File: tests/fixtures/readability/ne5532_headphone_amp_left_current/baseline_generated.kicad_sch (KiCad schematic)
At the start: 13 parts, among them J1 AudioIn_L, J2 AudioIn_R, J3 PowerSupply, J4 HeadphoneOut_L, J5 HeadphoneOut_R

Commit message: fix: improve layout regression handling
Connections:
- net VCC is gone; now on net GND: J3.1 (A), R3.1 (A), R3.2 (B)
- net GND: now also J4.1 (A), J4.2 (B), J5.1 (A), J5.2 (B), R4.1 (A), R4.2 (B), R7.2 (B), R8.2 (B)
- net at J1.1 (A), J1.2 (B), R1.1 (A): now also J3.2 (B)
- net at R2.2 (B): now also R6.1 (A), R7.1 (A), R8.1 (A)
- now unconnected: R1.2 (B), R5.1 (A), R5.2 (B)

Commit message: fix: stabilize graphviz layout regressions
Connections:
- net GND: now also J3.2 (B); no longer J2.1 (A), J2.2 (B), J3.1 (A), J4.1 (A), J4.2 (B), J5.1 (A), J5.2 (B), R2.1 (A), R3.1 (A), R3.2 (B), R4.1 (A), R7.2 (B), R8.2 (B)
- net at R2.2 (B), R6.1 (A), R8.1 (A): no longer R7.1 (A)
- net at J1.1 (A), J1.2 (B), R1.1 (A): no longer J3.2 (B)
- net VCC: now reaches R1.2 (B)
- net VCC: now also J3.1 (A), R3.1 (A), R3.2 (B), R4.1 (A), R5.1 (A), R7.1 (A)
- new net: J4.1 (A), J4.2 (B), R7.2 (B)
- new net: J2.1 (A), J2.2 (B), R2.1 (A)
- new net: J5.1 (A), J5.2 (B), R8.2 (B)

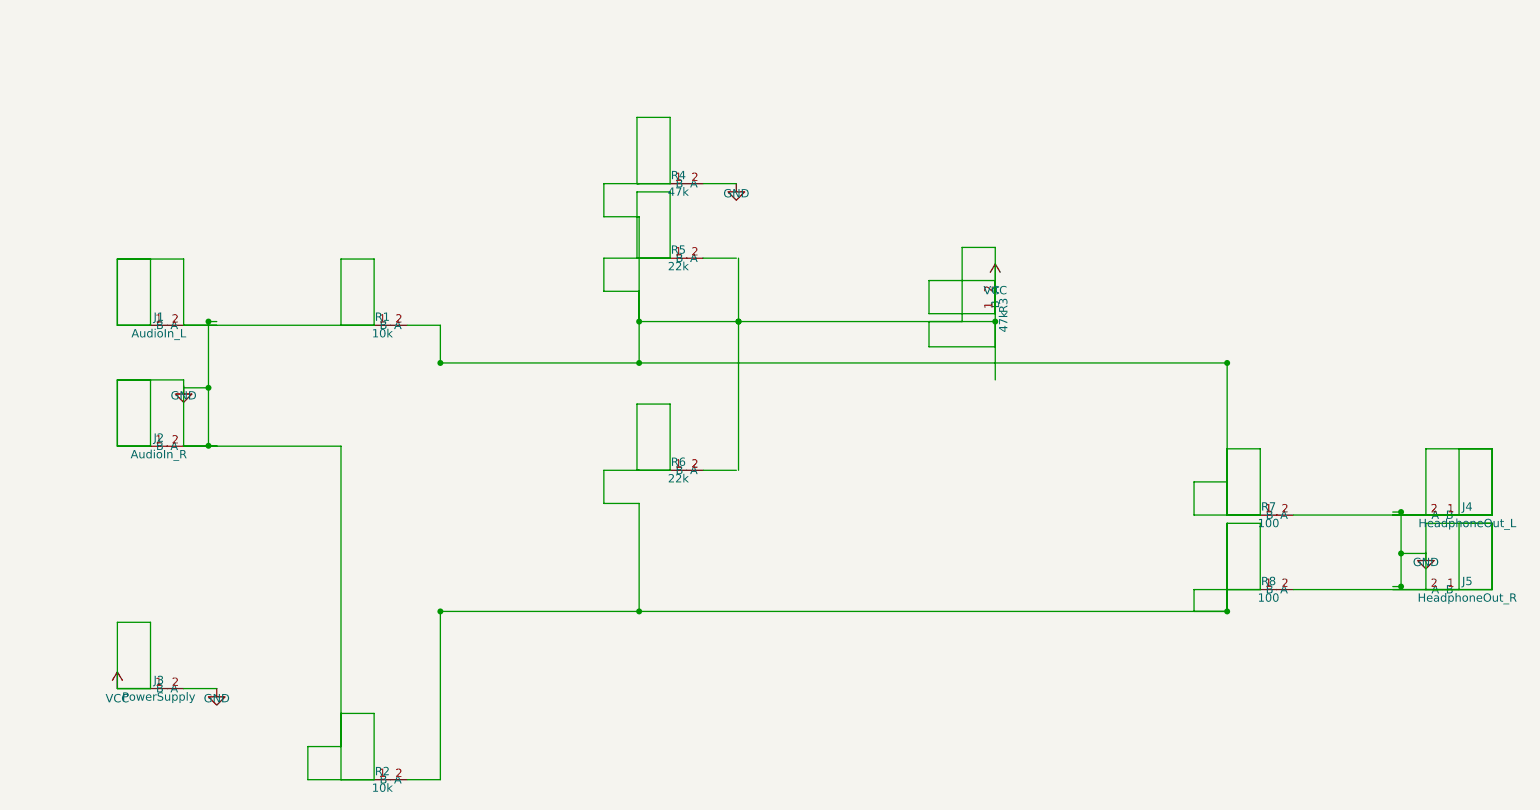
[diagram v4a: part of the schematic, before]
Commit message: fix: refine NE5532 routing geometry
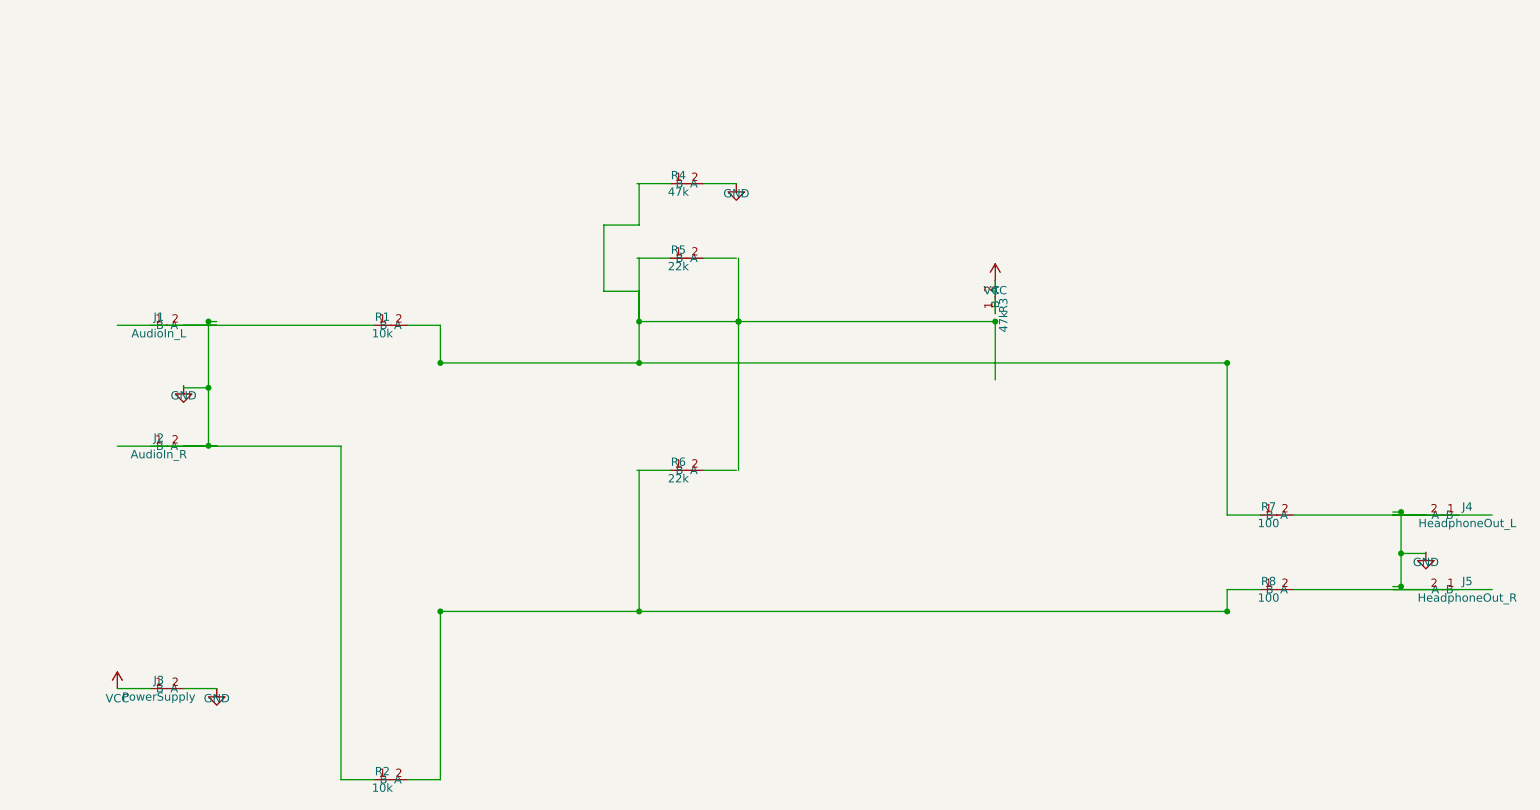
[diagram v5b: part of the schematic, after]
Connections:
- net VCC: no longer R1.2 (B), R4.1 (A), R5.1 (A), R7.1 (A)
- net at J2.2 (B), R2.1 (A): no longer J2.1 (A)
- net at J4.2 (B), R7.2 (B): no longer J4.1 (A)
- net at R2.2 (B), R8.1 (A): no longer R6.1 (A)
- net at J1.2 (B), R1.1 (A): no longer J1.1 (A)
- net at J5.2 (B), R8.2 (B): no longer J5.1 (A)
- new net: R1.2 (B), R7.1 (A)

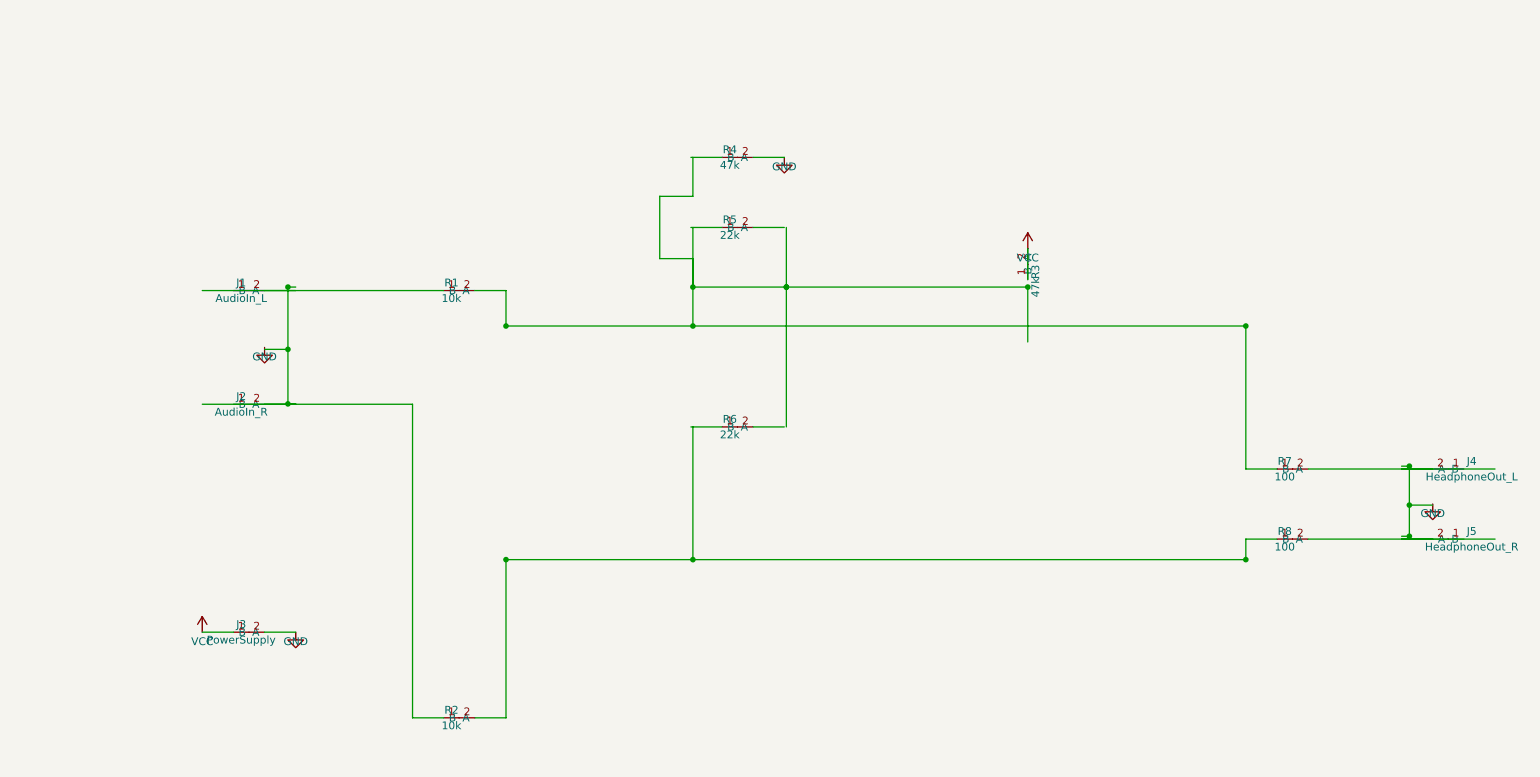
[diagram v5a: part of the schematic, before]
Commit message: fix: improve routing and label readability
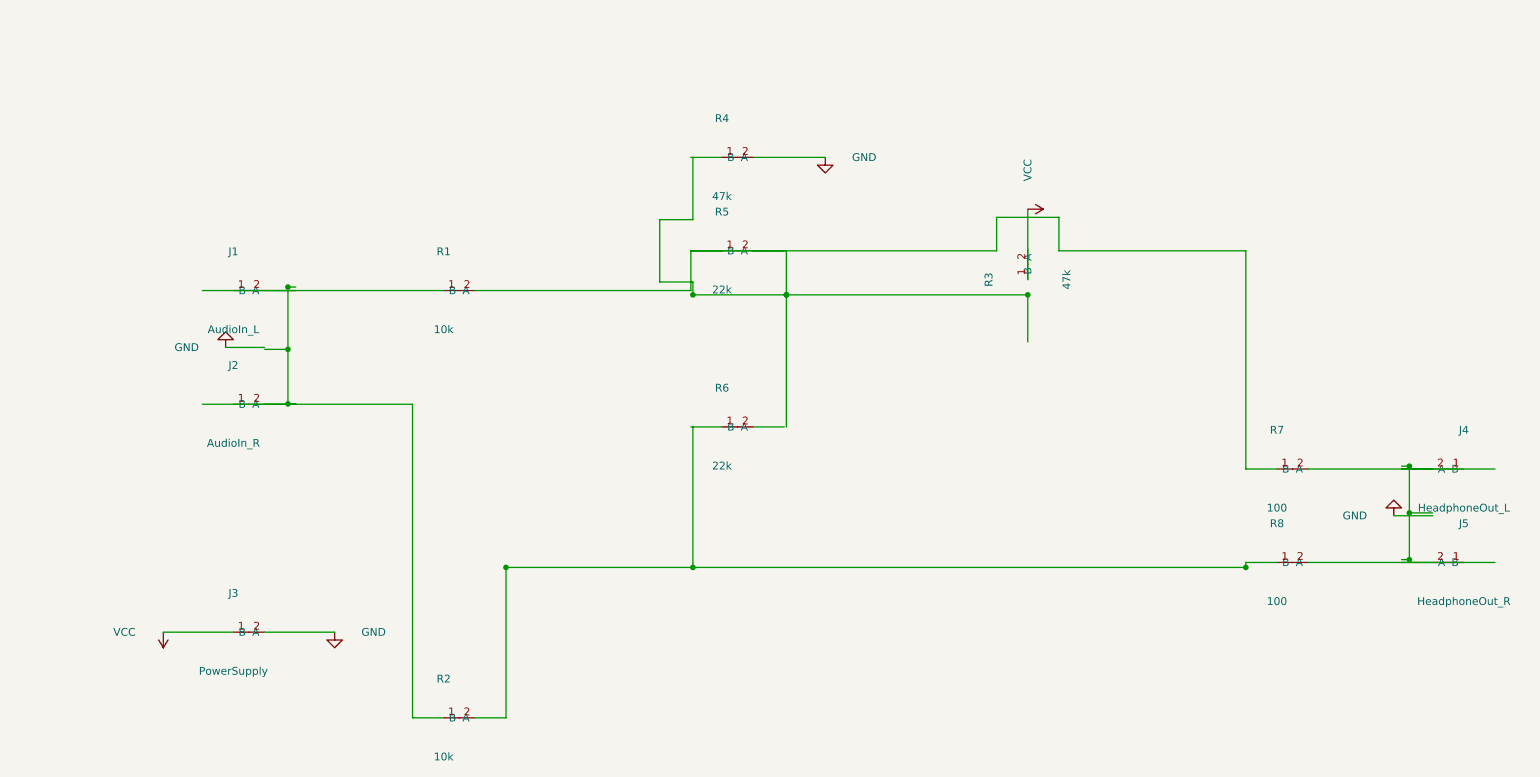
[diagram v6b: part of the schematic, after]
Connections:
- net VCC: no longer R3.2 (B)
- net at R1.2 (B), R7.1 (A): now also R5.1 (A), R5.2 (B)
